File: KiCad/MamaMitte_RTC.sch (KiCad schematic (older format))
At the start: 7 parts, among them U2 S3511A

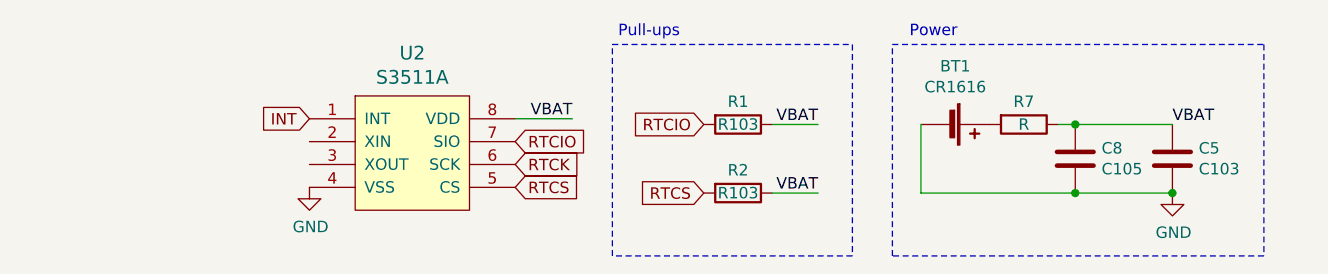
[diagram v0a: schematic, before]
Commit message: Update RTC schematic
Add crystal
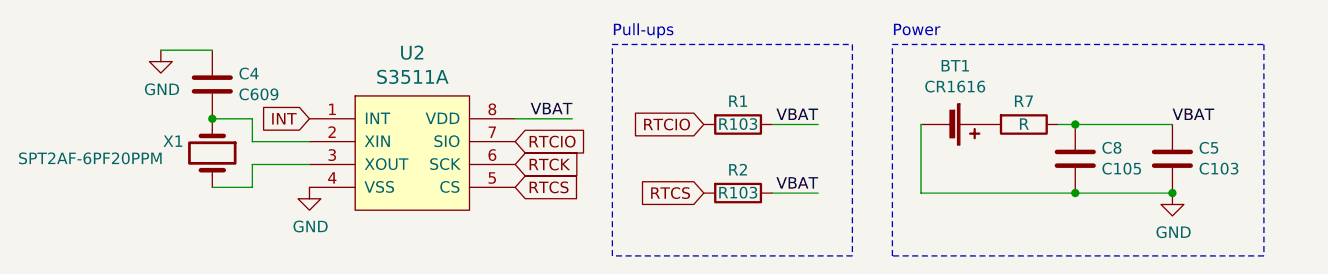
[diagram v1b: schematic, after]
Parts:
- added C4: C609, symbol Device:C
- added X1: SPT2AF-6PF20PPM, symbol MamaMitte:SPT2AF-6PF20PPM
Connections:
- net GND: now also C4.1
- net at U2.2 (XIN): now also C4.2, X1.1
- net at U2.3 (XOUT): now also X1.4
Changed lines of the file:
@@
 Wire Notes Line
 	5325 4075 5325 3150
-Text Notes 5350 3125 0    50   ~ 0
+Text Notes 5325 3125 0    50   ~ 0
 Pull-ups
 $Comp
@@
 Wire Notes Line
 	6550 4075 6550 3150
-Text Notes 6625 3125 0    50   ~ 0
+Text Notes 6550 3125 0    50   ~ 0
 Power
 Connection ~ 7775 3800
@@
 Wire Wire Line
 	6025 3500 6225 3500
+$Comp
+L Device:C C4
+U 1 1 607E4C2B
+P 3575 3325
+F 0 "C4" H 3690 3371 50  0000 L CNN
+F 1 "C609" H 3690 3280 50  0000 L CNN
+F 2 "" H 3613 3175 50  0001 C CNN
+F 3 "~" H 3575 3325 50  0001 C CNN
+	1    3575 3325
+	1    0    0    -1
+$EndComp
+$Comp
+L power:GND #PWR?
+U 1 1 607E5375
+P 3350 3175
+F 0 "#PWR?" H 3350 2925 50  0001 C CNN
+F 1 "GND" H 3355 3002 50  0000 C CNN
+F 2 "" H 3350 3175 50  0001 C CNN
+F 3 "" H 3350 3175 50  0001 C CNN
+	1    3350 3175
+	1    0    0    -1
+$EndComp
+Wire Wire Line
+	3350 3175 3575 3175
+Wire Wire Line
+	3575 3475 3750 3475
+Wire Wire Line
+	3750 3475 3750 3575
+Wire Wire Line
+	3750 3575 4000 3575
+Wire Wire Line
+	3575 3775 3750 3775
+Wire Wire Line
+	3750 3775 3750 3675
+Wire Wire Line
+	3750 3675 4000 3675
+$Comp
+L MamaMitte:SPT2AF-6PF20PPM X1
+U 1 1 607ED854
+P 3575 3625
+F 0 "X1" V 3525 3500 50  0000 R CNN
+F 1 "SPT2AF-6PF20PPM" V 3600 2775 50  0000 L CNN
+F 2 "" H 3575 3625 50  0001 C CNN
+F 3 "~" H 3575 3625 50  0001 C CNN
+	1    3575 3625
+	0    1    1    0
+$EndComp
+Connection ~ 3575 3475
 $EndSCHEMATC

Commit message: Add footprints and assign nets
Assigned and placed footprints, and assigned nets to vias.
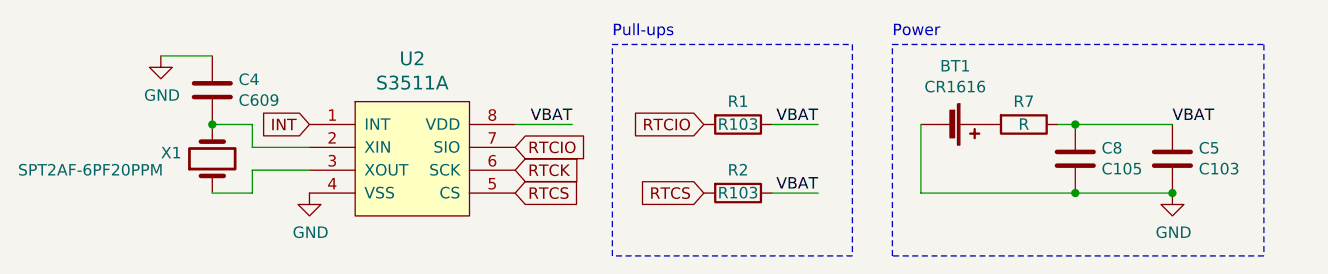
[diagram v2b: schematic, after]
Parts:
- BT1: footprint (none) -> MamaMitte:BatteryHolder_3N1_CR1616
- C4, C5, C8: footprint (none) -> MamaMitte:C_0402_1005Metric
- R1, R2, R7: footprint (none) -> MamaMitte:R_0402_1005Metric
- U2: footprint (none) -> MamaMitte:SSOP-8_4.4x3mm_P0.65mm
- X1: footprint (none) -> MamaMitte:Oscillator_SMD_SeikoEpson_SPT2AF-4Pin_8.7x3.7mm
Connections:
- net at C4.2, U2.2 (XIN): now also X1.4; no longer X1.1
- net at U2.3 (XOUT): now also X1.1; no longer X1.4
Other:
- moved on the sheet: C4, U2, X1
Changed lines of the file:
@@
 L MamaMitte:S3511A U2
 U 1 1 608ADF45
-P 4450 3625
-F 0 "U2" H 4450 4062 60  0000 C CNN
-F 1 "S3511A" H 4450 3956 60  0000 C CNN
-F 2 "" H 3900 4325 60  0001 C CNN
-F 3 "" H 3900 4325 60  0001 C CNN
-	1    4450 3625
-	1    0    0    -1
-$EndComp
-Text GLabel 4900 3575 2    50   Input ~ 0
+P 4450 3650
+F 0 "U2" H 4450 4087 60  0000 C CNN
+F 1 "S3511A" H 4450 3981 60  0000 C CNN
+F 2 "MamaMitte:SSOP-8_4.4x3mm_P0.65mm" H 3900 4350 60  0001 C CNN
+F 3 "" H 3900 4350 60  0001 C CNN
+	1    4450 3650
+	1    0    0    -1
+$EndComp
+Text GLabel 4900 3600 2    50   Input ~ 0
 RTCIO
-Text GLabel 4900 3675 2    50   Input ~ 0
+Text GLabel 4900 3700 2    50   Input ~ 0
 RTCK
-Text GLabel 4900 3775 2    50   Input ~ 0
+Text GLabel 4900 3800 2    50   Input ~ 0
 RTCS
-Text GLabel 4000 3475 0    50   Input ~ 0
+Text GLabel 4000 3500 0    50   Input ~ 0
 INT
 $Comp
@@
 F 0 "R1" V 5775 3500 50  0000 C CNN
 F 1 "R103" V 5875 3500 50  0000 C CNN
-F 2 "" V 5805 3500 50  0001 C CNN
+F 2 "MamaMitte:R_0402_1005Metric" V 5805 3500 50  0001 C CNN
 F 3 "~" H 5875 3500 50  0001 C CNN
 	1    5875 3500
@@
 F 0 "C5" H 7890 3696 50  0000 L CNN
 F 1 "C103" H 7890 3605 50  0000 L CNN
-F 2 "" H 7813 3500 50  0001 C CNN
+F 2 "MamaMitte:C_0402_1005Metric" H 7813 3500 50  0001 C CNN
 F 3 "~" H 7775 3650 50  0001 C CNN
 	1    7775 3650
@@
 F 0 "R2" V 5775 3800 50  0000 C CNN
 F 1 "R103" V 5875 3800 50  0000 C CNN
-F 2 "" V 5805 3800 50  0001 C CNN
+F 2 "MamaMitte:R_0402_1005Metric" V 5805 3800 50  0001 C CNN
 F 3 "~" H 5875 3800 50  0001 C CNN
 	1    5875 3800
@@
 RTCS
 $Comp
-L power:GND #PWR?
+L power:GND #PWR0112
 U 1 1 609AB4C4
-P 4000 3775
-F 0 "#PWR?" H 4000 3525 50  0001 C CNN
-F 1 "GND" H 4005 3602 50  0000 C CNN
-F 2 "" H 4000 3775 50  0001 C CNN
-F 3 "" H 4000 3775 50  0001 C CNN
-	1    4000 3775
-	1    0    0    -1
-$EndComp
-Wire Wire Line
-	4900 3475 5150 3475
+P 4000 3800
+F 0 "#PWR0112" H 4000 3550 50  0001 C CNN
+F 1 "GND" H 4005 3627 50  0000 C CNN
+F 2 "" H 4000 3800 50  0001 C CNN
+F 3 "" H 4000 3800 50  0001 C CNN
+	1    4000 3800
+	1    0    0    -1
+$EndComp
+Wire Wire Line
+	4900 3500 5150 3500
 $Comp
 L Device:Battery_Cell BT1
@@
 F 0 "BT1" V 6520 3550 50  0000 C CNN
 F 1 "CR1616" V 6611 3550 50  0000 C CNN
-F 2 "" V 6775 3560 50  0001 C CNN
+F 2 "MamaMitte:BatteryHolder_3N1_CR1616" V 6775 3560 50  0001 C CNN
 F 3 "~" V 6775 3560 50  0001 C CNN
 	1    6775 3500
@@
 $EndComp
 $Comp
-L power:GND #PWR?
+L power:GND #PWR0113
 U 1 1 60A6C168
 P 7775 3800
-F 0 "#PWR?" H 7775 3550 50  0001 C CNN
+F 0 "#PWR0113" H 7775 3550 50  0001 C CNN
 F 1 "GND" H 7780 3627 50  0000 C CNN
 F 2 "" H 7775 3800 50  0001 C CNN
@@
 F 0 "R7" V 7025 3500 50  0000 C CNN
 F 1 "R" V 7125 3500 50  0000 C CNN
-F 2 "" V 7055 3500 50  0001 C CNN
+F 2 "MamaMitte:R_0402_1005Metric" V 7055 3500 50  0001 C CNN
 F 3 "~" H 7125 3500 50  0001 C CNN
 	1    7125 3500
@@
 F 0 "C8" H 7465 3696 50  0000 L CNN
 F 1 "C105" H 7465 3605 50  0000 L CNN
-F 2 "" H 7388 3500 50  0001 C CNN
+F 2 "MamaMitte:C_0402_1005Metric" H 7388 3500 50  0001 C CNN
 F 3 "~" H 7350 3650 50  0001 C CNN
 	1    7350 3650
@@
 Wire Wire Line
 	7275 3500 7350 3500
-Text Label 5150 3475 2    50   ~ 0
+Text Label 5150 3500 2    50   ~ 0
 VBAT
 Wire Notes Line
@@
 L Device:C C4
 U 1 1 607E4C2B
-P 3575 3325
-F 0 "C4" H 3690 3371 50  0000 L CNN
-F 1 "C609" H 3690 3280 50  0000 L CNN
-F 2 "" H 3613 3175 50  0001 C CNN
-F 3 "~" H 3575 3325 50  0001 C CNN
-	1    3575 3325
-	1    0    0    -1
-$EndComp
-$Comp
-L power:GND #PWR?
+P 3575 3350
+F 0 "C4" H 3690 3396 50  0000 L CNN
+F 1 "C609" H 3690 3305 50  0000 L CNN
+F 2 "MamaMitte:C_0402_1005Metric" H 3613 3200 50  0001 C CNN
+F 3 "~" H 3575 3350 50  0001 C CNN
+	1    3575 3350
+	1    0    0    -1
+$EndComp
+$Comp
+L power:GND #PWR0114
 U 1 1 607E5375
-P 3350 3175
-F 0 "#PWR?" H 3350 2925 50  0001 C CNN
-F 1 "GND" H 3355 3002 50  0000 C CNN
-F 2 "" H 3350 3175 50  0001 C CNN
-F 3 "" H 3350 3175 50  0001 C CNN
-	1    3350 3175
-	1    0    0    -1
-$EndComp
-Wire Wire Line
-	3350 3175 3575 3175
-Wire Wire Line
-	3575 3475 3750 3475
-Wire Wire Line
-	3750 3475 3750 3575
-Wire Wire Line
-	3750 3575 4000 3575
-Wire Wire Line
-	3575 3775 3750 3775
-Wire Wire Line
-	3750 3775 3750 3675
-Wire Wire Line
-	3750 3675 4000 3675
+P 3350 3200
+F 0 "#PWR0114" H 3350 2950 50  0001 C CNN
+F 1 "GND" H 3355 3027 50  0000 C CNN
+F 2 "" H 3350 3200 50  0001 C CNN
+F 3 "" H 3350 3200 50  0001 C CNN
+	1    3350 3200
+	1    0    0    -1
+$EndComp
+Wire Wire Line
+	3350 3200 3575 3200
+Wire Wire Line
+	3575 3500 3750 3500
+Wire Wire Line
+	3750 3500 3750 3600
+Wire Wire Line
+	3750 3600 4000 3600
+Wire Wire Line
+	3575 3800 3750 3800
+Wire Wire Line
+	3750 3800 3750 3700
+Wire Wire Line
+	3750 3700 4000 3700
 $Comp
 L MamaMitte:SPT2AF-6PF20PPM X1
 U 1 1 607ED854
-P 3575 3625
-F 0 "X1" V 3525 3500 50  0000 R CNN
-F 1 "SPT2AF-6PF20PPM" V 3600 2775 50  0000 L CNN
-F 2 "" H 3575 3625 50  0001 C CNN
-F 3 "~" H 3575 3625 50  0001 C CNN
-	1    3575 3625
-	0    1    1    0
-$EndComp
-Connection ~ 3575 3475
+P 3575 3650
+F 0 "X1" V 3600 3875 50  0000 R CNN
+F 1 "SPT2AF-6PF20PPM" V 3525 4500 50  0000 R CNN
+F 2 "MamaMitte:Oscillator_SMD_SeikoEpson_SPT2AF-4Pin_8.7x3.7mm" H 3575 3650 50  0001 C CNN
+F 3 "~" H 3575 3650 50  0001 C CNN
+	1    3575 3650
+	0    -1   -1   0
+$EndComp
+Connection ~ 3575 3500
 $EndSCHEMATC

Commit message: Update schematic
Fix Bandai 2003 pinout and RTC power.
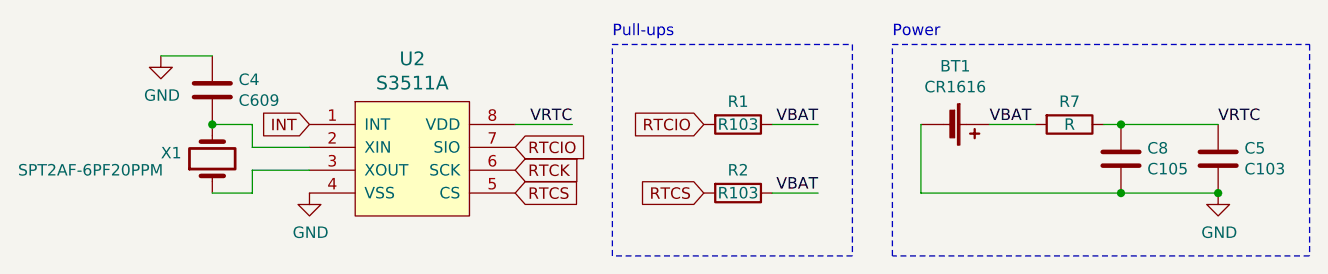
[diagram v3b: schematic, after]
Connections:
- net VBAT: now also BT1.1 (+), R7.2; no longer C5.1, C8.1, R7.1, U2.8 (VDD)
- new net VRTC: C5.1, C8.1, R7.1, U2.8 (VDD)
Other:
- moved on the sheet: C5, C8, R7
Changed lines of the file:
@@
 Pull-ups
-$Comp
-L Device:C C5
-U 1 1 609A6AFA
-P 7775 3650
-F 0 "C5" H 7890 3696 50  0000 L CNN
-F 1 "C103" H 7890 3605 50  0000 L CNN
-F 2 "MamaMitte:C_0402_1005Metric" H 7813 3500 50  0001 C CNN
-F 3 "~" H 7775 3650 50  0001 C CNN
-	1    7775 3650
-	1    0    0    -1
-$EndComp
 $Comp
 L Device:R R2
@@
 	0    1    1    0
 $EndComp
-$Comp
-L power:GND #PWR0113
-U 1 1 60A6C168
-P 7775 3800
-F 0 "#PWR0113" H 7775 3550 50  0001 C CNN
-F 1 "GND" H 7780 3627 50  0000 C CNN
-F 2 "" H 7775 3800 50  0001 C CNN
-F 3 "" H 7775 3800 50  0001 C CNN
-	1    7775 3800
-	1    0    0    -1
-$EndComp
-$Comp
-L Device:R R7
-U 1 1 60A744DC
-P 7125 3500
-F 0 "R7" V 7025 3500 50  0000 C CNN
-F 1 "R" V 7125 3500 50  0000 C CNN
-F 2 "MamaMitte:R_0402_1005Metric" V 7055 3500 50  0001 C CNN
-F 3 "~" H 7125 3500 50  0001 C CNN
-	1    7125 3500
-	0    1    1    0
-$EndComp
-$Comp
-L Device:C C8
-U 1 1 60A791F0
-P 7350 3650
-F 0 "C8" H 7465 3696 50  0000 L CNN
-F 1 "C105" H 7465 3605 50  0000 L CNN
-F 2 "MamaMitte:C_0402_1005Metric" H 7388 3500 50  0001 C CNN
-F 3 "~" H 7350 3650 50  0001 C CNN
-	1    7350 3650
-	1    0    0    -1
-$EndComp
 Wire Wire Line
 	6675 3800 6675 3500
-Text Label 7775 3500 0    50   ~ 0
-VBAT
-Wire Wire Line
-	7275 3500 7350 3500
 Text Label 5150 3500 2    50   ~ 0
-VBAT
+VRTC
 Wire Notes Line
-	6550 3150 8175 3150
+	6550 3150 8375 3150
 Wire Notes Line
-	8175 3150 8175 4075
+	8375 3150 8375 4075
 Wire Notes Line
-	8175 4075 6550 4075
+	8375 4075 6550 4075
 Wire Notes Line
 	6550 4075 6550 3150
 Text Notes 6550 3125 0    50   ~ 0
 Power
-Connection ~ 7775 3800
-Connection ~ 7350 3500
-Wire Wire Line
-	7350 3500 7775 3500
-Connection ~ 7350 3800
-Wire Wire Line
-	7350 3800 7775 3800
-Wire Wire Line
-	6675 3800 7350 3800
 Text Label 6225 3500 2    50   ~ 0
 VBAT
@@
 $EndComp
 Connection ~ 3575 3500
+Text Label 6975 3500 0    50   ~ 0
+VBAT
+Wire Wire Line
+	6675 3800 7550 3800
+Wire Wire Line
+	7550 3800 7975 3800
+Connection ~ 7550 3800
+Wire Wire Line
+	7550 3500 7975 3500
+Connection ~ 7550 3500
+Connection ~ 7975 3800
+Wire Wire Line
+	7475 3500 7550 3500
+Text Label 7975 3500 0    50   ~ 0
+VRTC
+$Comp
+L Device:C C8
+U 1 1 60A791F0
+P 7550 3650
+F 0 "C8" H 7665 3696 50  0000 L CNN
+F 1 "C105" H 7665 3605 50  0000 L CNN
+F 2 "MamaMitte:C_0402_1005Metric" H 7588 3500 50  0001 C CNN
+F 3 "~" H 7550 3650 50  0001 C CNN
+	1    7550 3650
+	1    0    0    -1
+$EndComp
+$Comp
+L Device:R R7
+U 1 1 60A744DC
+P 7325 3500
+F 0 "R7" V 7225 3500 50  0000 C CNN
+F 1 "R" V 7325 3500 50  0000 C CNN
+F 2 "MamaMitte:R_0402_1005Metric" V 7255 3500 50  0001 C CNN
+F 3 "~" H 7325 3500 50  0001 C CNN
+	1    7325 3500
+	0    1    1    0
+$EndComp
+$Comp
+L power:GND #PWR0113
+U 1 1 60A6C168
+P 7975 3800
+F 0 "#PWR0113" H 7975 3550 50  0001 C CNN
+F 1 "GND" H 7980 3627 50  0000 C CNN
+F 2 "" H 7975 3800 50  0001 C CNN
+F 3 "" H 7975 3800 50  0001 C CNN
+	1    7975 3800
+	1    0    0    -1
+$EndComp
+$Comp
+L Device:C C5
+U 1 1 609A6AFA
+P 7975 3650
+F 0 "C5" H 8090 3696 50  0000 L CNN
+F 1 "C103" H 8090 3605 50  0000 L CNN
+F 2 "MamaMitte:C_0402_1005Metric" H 8013 3500 50  0001 C CNN
+F 3 "~" H 7975 3650 50  0001 C CNN
+	1    7975 3650
+	1    0    0    -1
+$EndComp
+Wire Wire Line
+	6975 3500 7175 3500
 $EndSCHEMATC

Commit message: Update schematic
Change power source for RTC pull-ups, and restructure IR block.
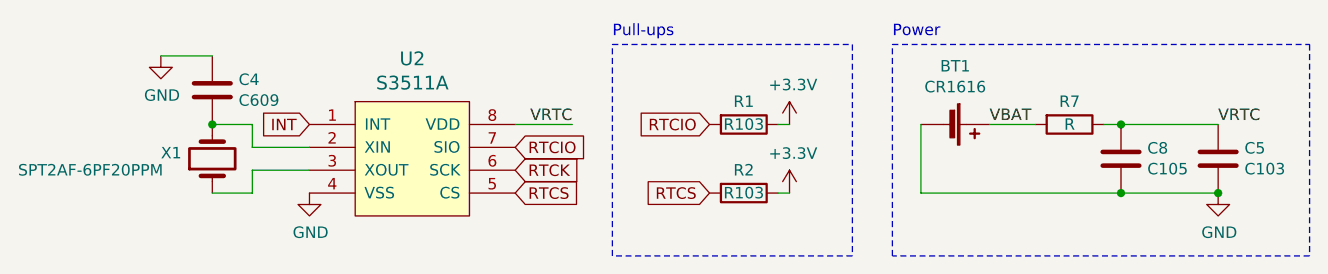
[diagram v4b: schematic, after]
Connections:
- net VBAT: no longer R1.1, R2.1
- new net +3V3: R1.1, R2.1
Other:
- moved on the sheet: R1, R2
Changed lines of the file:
@@
 L Device:R R1
 U 1 1 60997854
-P 5875 3500
-F 0 "R1" V 5775 3500 50  0000 C CNN
-F 1 "R103" V 5875 3500 50  0000 C CNN
-F 2 "MamaMitte:R_0402_1005Metric" V 5805 3500 50  0001 C CNN
-F 3 "~" H 5875 3500 50  0001 C CNN
-	1    5875 3500
-	0    1    1    0
-$EndComp
-Text GLabel 5725 3500 0    50   Input ~ 0
+P 5900 3500
+F 0 "R1" V 5800 3500 50  0000 C CNN
+F 1 "R103" V 5900 3500 50  0000 C CNN
+F 2 "MamaMitte:R_0402_1005Metric" V 5830 3500 50  0001 C CNN
+F 3 "~" H 5900 3500 50  0001 C CNN
+	1    5900 3500
+	0    1    1    0
+$EndComp
+Text GLabel 5750 3500 0    50   Input ~ 0
 RTCIO
 Wire Notes Line
@@
 L Device:R R2
 U 1 1 609A8C87
-P 5875 3800
-F 0 "R2" V 5775 3800 50  0000 C CNN
-F 1 "R103" V 5875 3800 50  0000 C CNN
-F 2 "MamaMitte:R_0402_1005Metric" V 5805 3800 50  0001 C CNN
-F 3 "~" H 5875 3800 50  0001 C CNN
-	1    5875 3800
-	0    1    1    0
-$EndComp
-Text GLabel 5725 3800 0    50   Input ~ 0
+P 5900 3800
+F 0 "R2" V 5800 3800 50  0000 C CNN
+F 1 "R103" V 5900 3800 50  0000 C CNN
+F 2 "MamaMitte:R_0402_1005Metric" V 5830 3800 50  0001 C CNN
+F 3 "~" H 5900 3800 50  0001 C CNN
+	1    5900 3800
+	0    1    1    0
+$EndComp
+Text GLabel 5750 3800 0    50   Input ~ 0
 RTCS
 $Comp
@@
 Text Notes 6550 3125 0    50   ~ 0
 Power
-Text Label 6225 3500 2    50   ~ 0
-VBAT
-Text Label 6225 3800 2    50   ~ 0
-VBAT
-Wire Wire Line
-	6025 3800 6225 3800
-Wire Wire Line
-	6025 3500 6225 3500
 $Comp
 L Device:C C4
@@
 Wire Wire Line
 	6975 3500 7175 3500
+$Comp
+L power:+3.3V #PWR?
+U 1 1 6091AED2
+P 6100 3500
+F 0 "#PWR?" H 6100 3350 50  0001 C CNN
+F 1 "+3.3V" H 6115 3673 50  0000 C CNN
+F 2 "" H 6100 3500 50  0001 C CNN
+F 3 "" H 6100 3500 50  0001 C CNN
+	1    6100 3500
+	1    0    0    -1
+$EndComp
+$Comp
+L power:+3.3V #PWR?
+U 1 1 6091D767
+P 6100 3800
+F 0 "#PWR?" H 6100 3650 50  0001 C CNN
+F 1 "+3.3V" H 6115 3973 50  0000 C CNN
+F 2 "" H 6100 3800 50  0001 C CNN
+F 3 "" H 6100 3800 50  0001 C CNN
+	1    6100 3800
+	1    0    0    -1
+$EndComp
+Wire Wire Line
+	6050 3500 6100 3500
+Wire Wire Line
+	6050 3800 6100 3800
 $EndSCHEMATC
